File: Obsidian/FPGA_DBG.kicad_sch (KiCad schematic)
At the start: 21 parts, among them Q3 BSS138LT1G, SW1 SW_DIP_x01, U1 XC7A35T-CSG325, U27 W25Q128JVFIQ, U9 REF3012

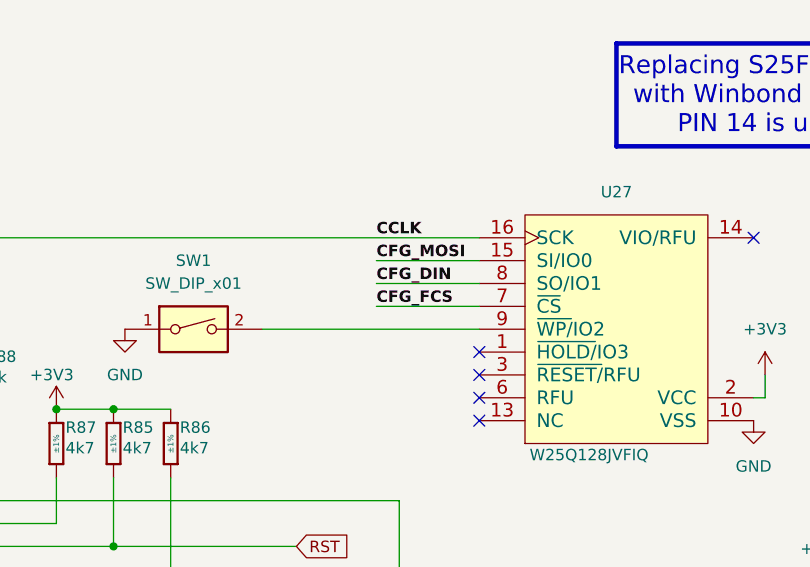
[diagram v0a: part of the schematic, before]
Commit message: adding return GND for quad-spi flash
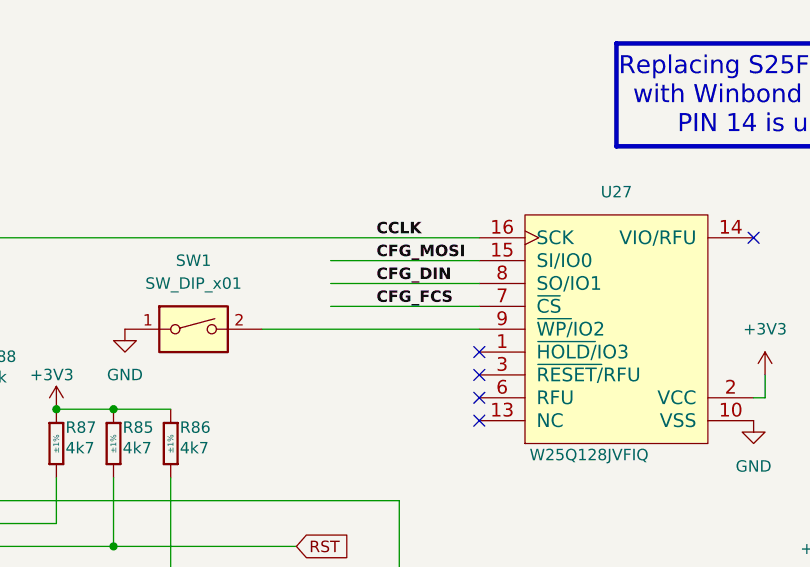
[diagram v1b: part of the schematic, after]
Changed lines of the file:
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@@
-	(wire
-		(pts
-			(xy 204.47 67.31) (xy 215.9 67.31)
-		)
-		(stroke
-			(width 0)
-			(type default)
-		)
-	)
 	(wire
 		(pts
@@
 	(wire
 		(pts
-			(xy 204.47 72.39) (xy 215.9 72.39)
-		)
-		(stroke
-			(width 0)
-			(type default)
-		)
-	)
-	(wire
-		(pts
 			(xy 162.56 147.32) (xy 167.64 147.32)
 		)
@@
 	(wire
 		(pts
+			(xy 199.39 72.39) (xy 215.9 72.39)
+		)
+		(stroke
+			(width 0)
+			(type default)
+		)
+	)
+	(wire
+		(pts
 			(xy 121.92 96.52) (xy 168.91 96.52)
 		)
@@
 	(wire
 		(pts
+			(xy 199.39 69.85) (xy 215.9 69.85)
+		)
+		(stroke
+			(width 0)
+			(type default)
+		)
+	)
+	(wire
+		(pts
 			(xy 121.92 124.46) (xy 121.92 127)
 		)
@@
 	(wire
 		(pts
+			(xy 199.39 67.31) (xy 215.9 67.31)
+		)
+		(stroke
+			(width 0)
+			(type default)
+		)
+	)
+	(wire
+		(pts
 			(xy 140.97 116.84) (xy 140.97 119.38)
 		)
@@
 		(pts
 			(xy 247.65 80.01) (xy 247.65 82.55)
-		)
-		(stroke
-			(width 0)
-			(type default)
-		)
-	)
-	(wire
-		(pts
-			(xy 204.47 69.85) (xy 215.9 69.85)
 		)
 		(stroke
@@
 		)
 	)
+	(netclass_flag ""
+		(length 1.27)
+		(shape round)
+		(at 199.39 64.77 0)
+		(fields_autoplaced yes)
+		(effects
+			(font
+				(size 1.27 1.27)
+			)
+			(justify left bottom)
+		)
+		(property "Netclass" "SPI"
+			(at 200.0885 63.5 0)
+			(effects
+				(font
+					(size 1.27 1.27)
+				)
+				(justify left)
+			)
+		)
+		(property "Component Class" ""
+			(at -54.61 -10.16 0)
+			(effects
+				(font
+					(size 1.27 1.27)
+					(italic yes)
+				)
+			)
+		)
+	)
+	(netclass_flag ""
+		(length 1.27)
+		(shape round)
+		(at 199.39 67.31 0)
+		(fields_autoplaced yes)
+		(effects
+			(font
+				(size 1.27 1.27)
+			)
+			(justify left bottom)
+		)
+		(property "Netclass" "SPI"
+			(at 200.0885 66.04 0)
+			(effects
+				(font
+					(size 1.27 1.27)
+				)
+				(justify left)
+			)
+		)
+		(property "Component Class" ""
+			(at -54.61 -7.62 0)
+			(effects
+				(font
+					(size 1.27 1.27)
+					(italic yes)
+				)
+			)
+		)
+	)
+	(netclass_flag ""
+		(length 1.27)
+		(shape round)
+		(at 199.39 69.85 0)
+		(fields_autoplaced yes)
+		(effects
+			(font
+				(size 1.27 1.27)
+			)
+			(justify left bottom)
+		)
+		(property "Netclass" "SPI"
+			(at 200.0885 68.58 0)
+			(effects
+				(font
+					(size 1.27 1.27)
+				)
+				(justify left)
+			)
+		)
+		(property "Component Class" ""
+			(at -54.61 -5.08 0)
+			(effects
+				(font
+					(size 1.27 1.27)
+					(italic yes)
+				)
+			)
+		)
+	)
+	(netclass_flag ""
+		(length 1.27)
+		(shape round)
+		(at 199.39 72.39 0)
+		(fields_autoplaced yes)
+		(effects
+			(font
+				(size 1.27 1.27)
+			)
+			(justify left bottom)
+		)
+		(property "Netclass" "SPI"
+			(at 200.0885 71.12 0)
+			(effects
+				(font
+					(size 1.27 1.27)
+				)
+				(justify left)
+			)
+		)
+		(property "Component Class" ""
+			(at -54.61 -2.54 0)
+			(effects
+				(font
+					(size 1.27 1.27)
+					(italic yes)
+				)
+			)
+		)
+	)

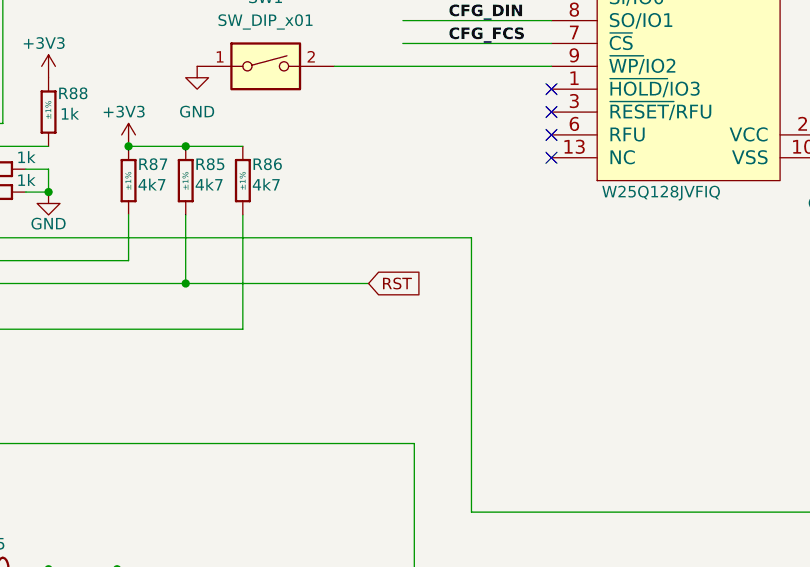
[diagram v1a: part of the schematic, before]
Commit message: removing reset global label
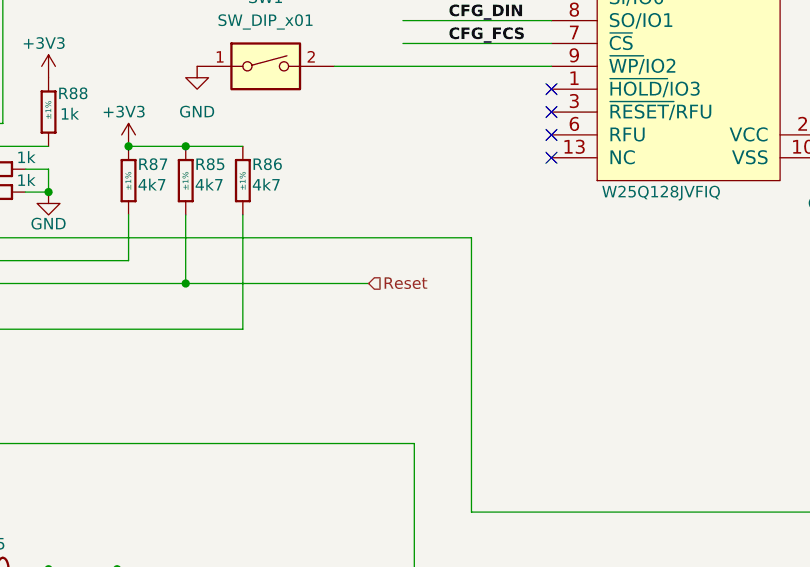
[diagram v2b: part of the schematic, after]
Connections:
- net RST renamed Reset
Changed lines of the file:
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@@
 		)
 	)
-	(global_label "RST"
+	(hierarchical_label "Reset"
 		(shape input)
 		(at 195.58 99.06 0)
-		(fields_autoplaced yes)
 		(effects
 			(font
@@
 			(justify left)
 		)
-		(property "Intersheetrefs" "${INTERSHEET_REFS}"
-			(at 202.0123 99.06 0)
-			(effects
-				(font
-					(size 1.27 1.27)
-				)
-				(justify left)
-				(hide yes)
-			)
-		)
 	)

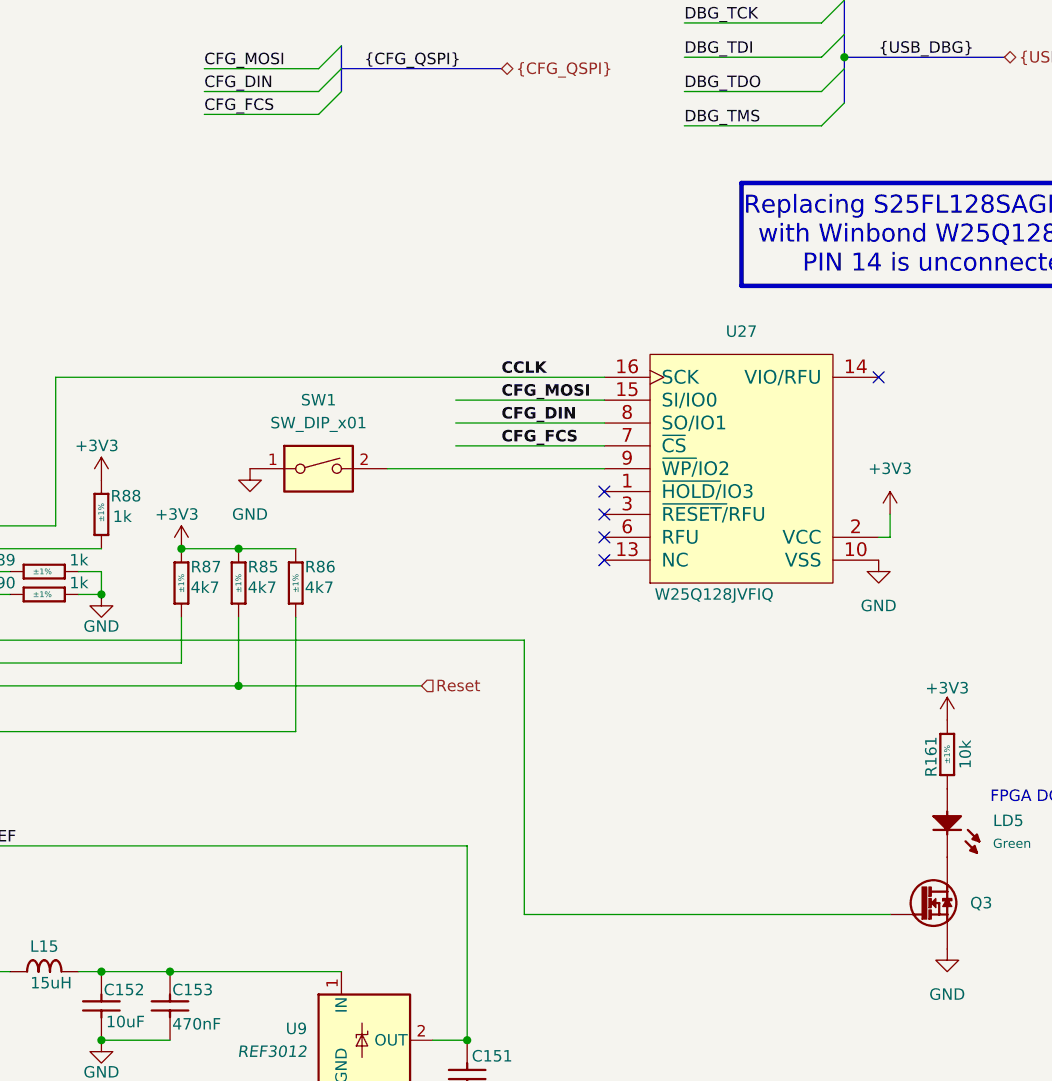
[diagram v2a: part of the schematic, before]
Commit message: Modifying line voltage for certain components, adding pull up resistor
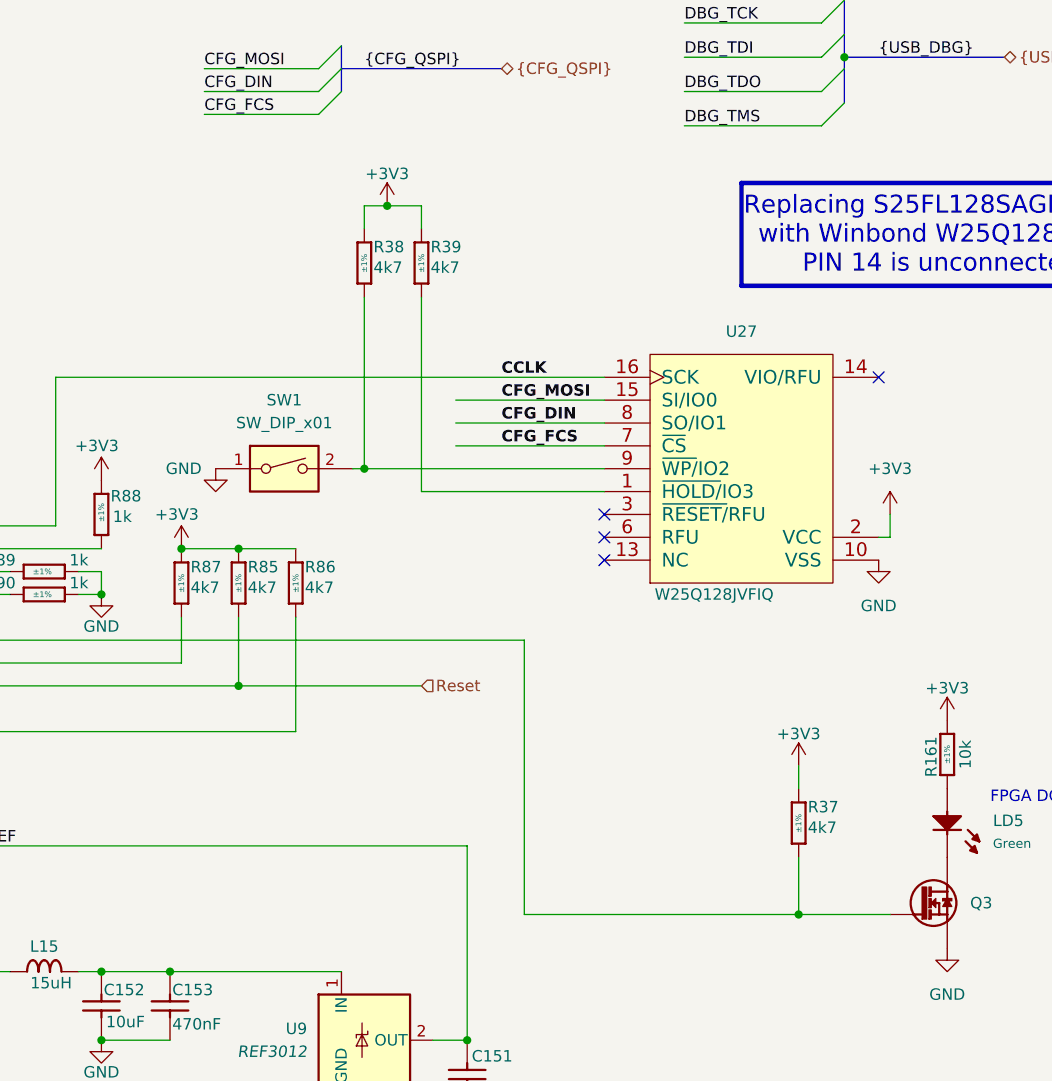
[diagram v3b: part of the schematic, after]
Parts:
- added R37, R38, R39: R0402_4K7_1%_0.0625W_100PPM, Footprint:RESC1005X40N, symbol Library_Symbol:R0402_4K7_1%_0.0625W_100PPM
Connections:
- net +3V3: now also R37.2, R38.2, R39.2
- net at Q3.1 (G), U1.F12 (DONE_0): now also R37.1
- net at SW1.2, U27.9 (~{WP/}IO2): now also R38.1
- net at U27.1 (~{HOLD/}IO3): now also R39.1
- no-connect marks 5 -> 4
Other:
- moved on the sheet: SW1

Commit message: update LCSC reference, and OFFSET rotation for JLCPCB
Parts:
- LD5: LCSC C5879295 -> C598257
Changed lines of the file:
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@@
 			)
 		)
-		(property "LCSC" "C5879295"
+		(property "LCSC" "C598257"
 			(at 254 114.3 90)
 			(effects

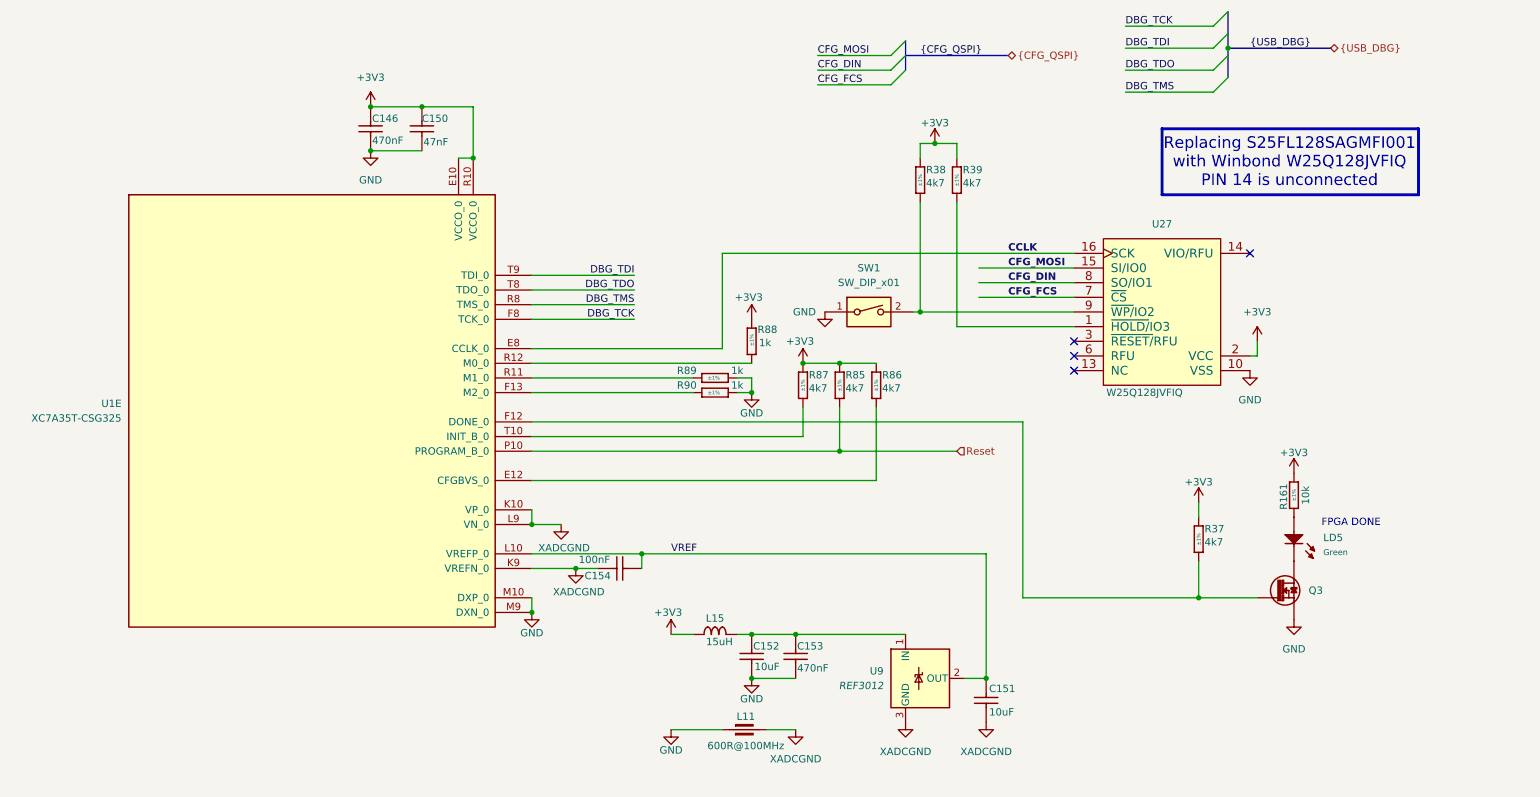
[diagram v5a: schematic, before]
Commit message: Adding documentation for configuration with flash memory, adding more comments to schematic
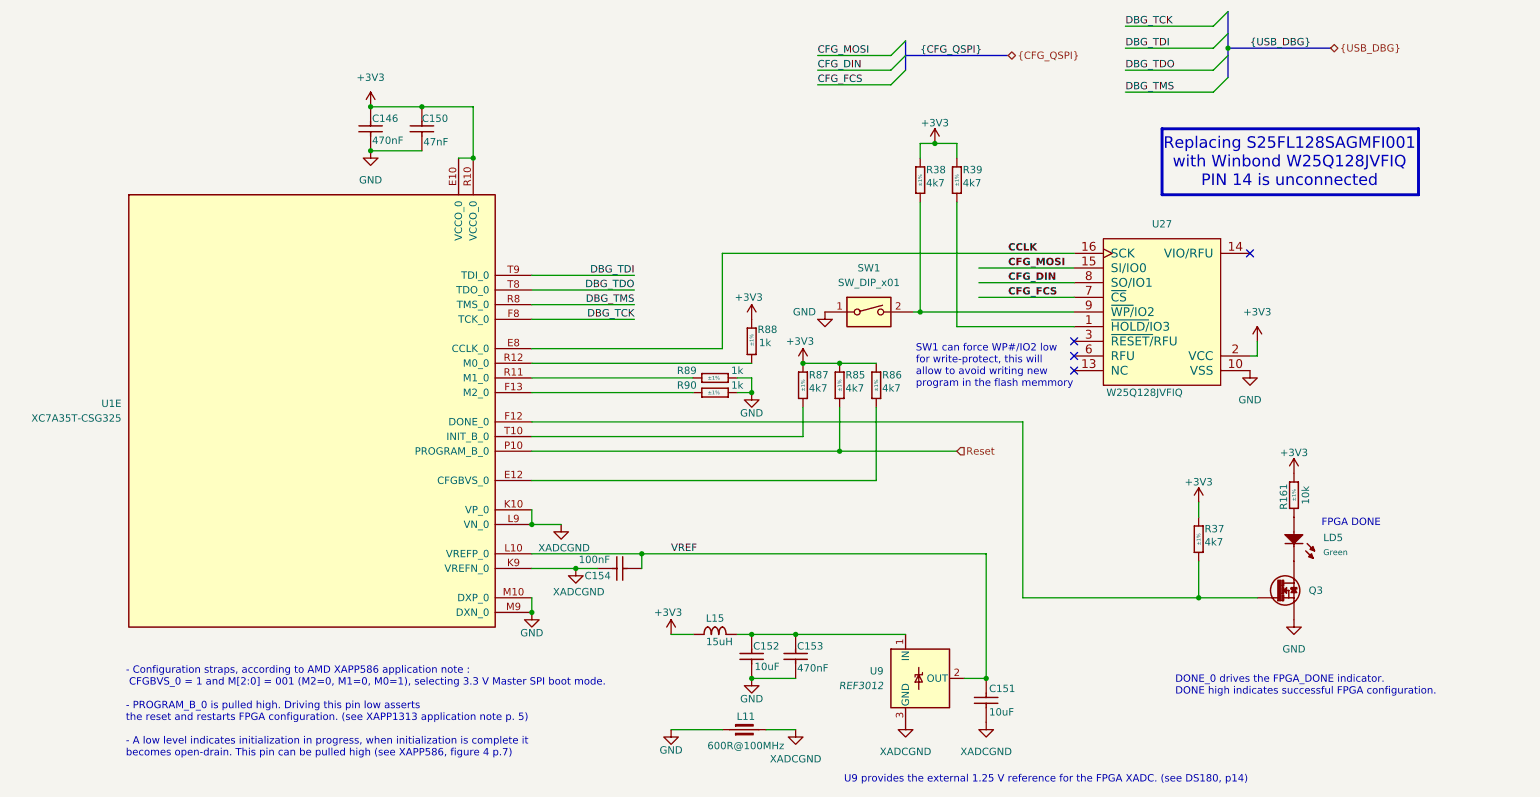
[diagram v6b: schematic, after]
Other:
- note added: "- Configuration straps, according to AMD XAPP586 application note : CFGBVS_0 = 1 and M[2:0] = 001 (M2=0, M1=0, M0=1), selecting 3.3 V Master SPI boot mode. - PROGRAM_B_0 is pulled high. Driving this pin low asserts the reset and restarts FPGA configuration. (see XAPP1313 application note p. 5) - A low level indicates initialization in progress, when initialization is complete it becomes open-drai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"
- note added: "DONE_0 drives the FPGA_DONE indicator. DONE high indicates successful FPGA configuration."
- note added: "SW1 can force WP#/IO2 low for write-protect, this will allow to avoid writing new program in the flash memmory"
- note added: "U9 provides the external 1.25 V reference for the FPGA XADC. (see DS180, p14)"
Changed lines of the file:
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@@
+		)
+	)
+	(text "U9 provides the external 1.25 V reference for the FPGA XADC. (see DS180, p14)\n"
+		(exclude_from_sim no)
+		(at 176.022 155.956 0)
+		(effects
+			(font
+				(size 1.27 1.27)
+			)
+			(justify left)
 		)
 	)
@@
 		)
 	)
+	(text "- Configuration straps, according to AMD XAPP586 application note :\n CFGBVS_0 = 1 and M[2:0] = 001 (M2=0, M1=0, M0=1), selecting 3.3 V Master SPI boot mode.\n\n- PROGRAM_B_0 is pulled high. Driving this pin low asserts \nthe reset and restarts FPGA configuration. (see XAPP1313 application note p. 5)\n\n- A low level indicates initialization in progress, when initialization is complete it\nbecomes open-drain. This pin can be pulled high (see XAPP586, figure 4 p.7) "
+		(exclude_from_sim no)
+		(at 51.562 144.272 0)
+		(effects
+			(font
+				(face "Arial")
+				(size 1.27 1.27)
+			)
+			(justify left)
+		)
+	)
+	(text "DONE_0 drives the FPGA_DONE indicator. \nDONE high indicates successful FPGA configuration."
+		(exclude_from_sim no)
+		(at 233.426 139.7 0)
+		(effects
+			(font
+				(face "Arial")
+				(size 1.27 1.27)
+			)
+			(justify left)
+		)
+	)
+	(text "SW1 can force WP#/IO2 low \nfor write-protect, this will \nallow to avoid writing new\nprogram in the flash memmory"
+		(exclude_from_sim no)
+		(at 188.468 84.328 0)
+		(effects
+			(font
+				(face "Arial")
+				(size 1.27 1.27)
+			)
+			(justify left)
+		)
+	)

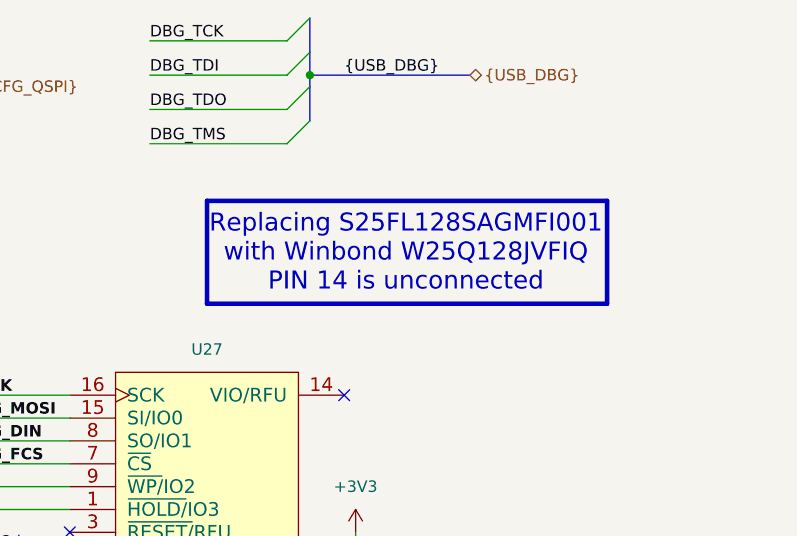
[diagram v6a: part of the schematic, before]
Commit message: adding comments, and test point for U12 (power supply in clock sheet)
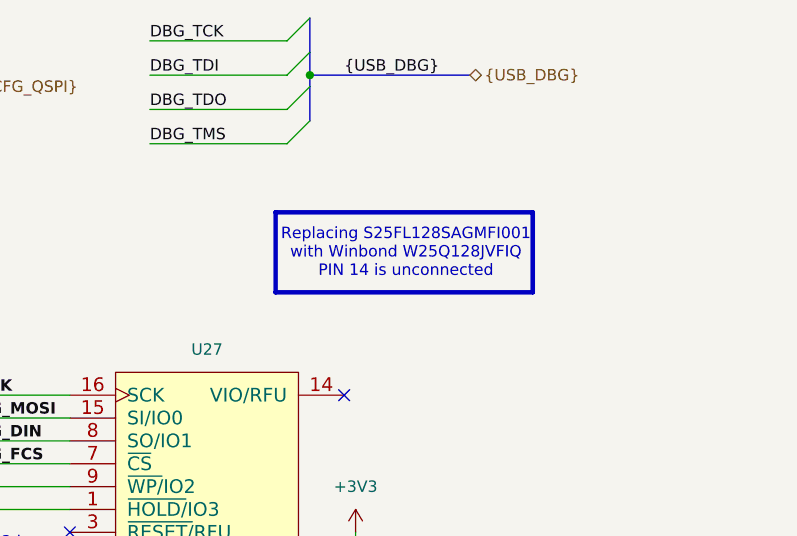
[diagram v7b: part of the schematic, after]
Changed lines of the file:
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@@
 	)
 	(rectangle
-		(start 231.14 43.18)
-		(end 275.59 54.61)
+		(start 238.76 44.45)
+		(end 267.335 53.34)
 		(stroke
 			(width 0.5)
@@
 		(effects
 			(font
-				(size 2 2)
+				(size 1.27 1.27)
 			)
 		)
